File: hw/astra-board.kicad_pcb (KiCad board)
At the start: 2 copper layers, 60 x 40 mm, 53 parts, among them J1 USB-C, J2 QWIIC, J3 OLED, J4 EXPANSION, Q1 S8050, SW1 USER1, SW2 USER2, SW3 RESET, SW4 BOOT, U1 ESP32-C3-WROOM-02-N4, U2 AMS1117-3.3, U3 74AHCT1G125, U4 USBLC6-2SC6

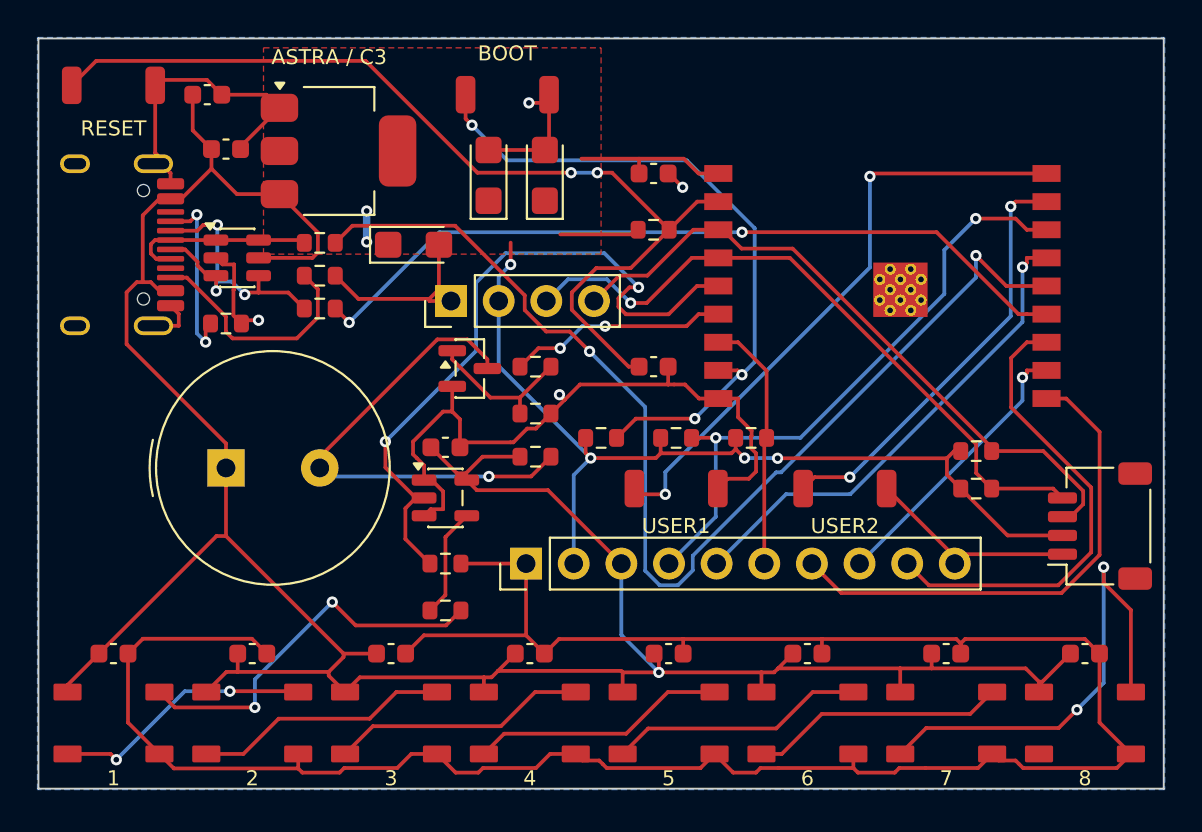
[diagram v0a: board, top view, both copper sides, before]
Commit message: Revise USB placement and power copper; regenerate verified fabrication package
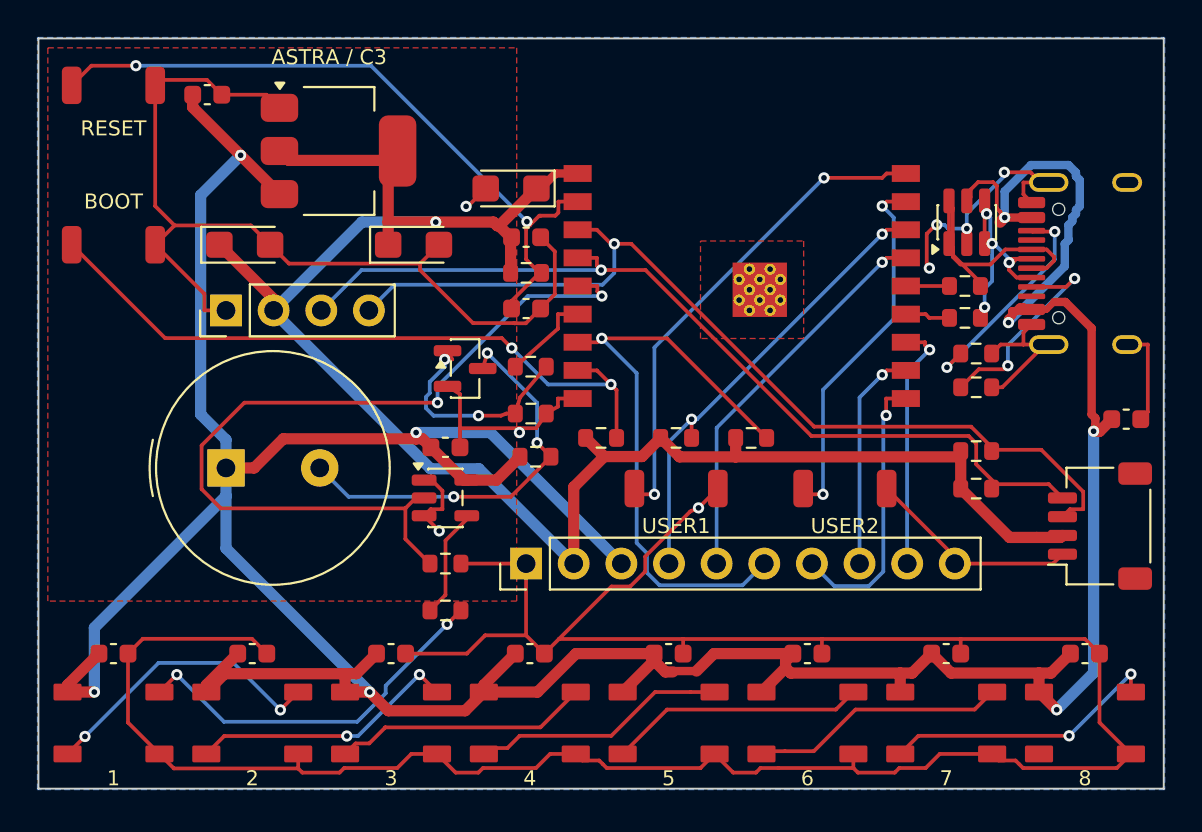
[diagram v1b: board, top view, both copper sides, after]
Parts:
- moved J1 54.0 mm to (157.0, 112.0), turned to 90 degrees
- moved C7 50.1 mm to (158.0, 120.3)
- moved R1 40.1 mm to (150.0, 118.6)
- moved U4 38.9 mm to (149.5, 109.8), turned to 90 degrees
- moved R2 35.2 mm to (150.0, 116.8)
- moved R14 34.5 mm to (149.4, 113.2), turned to 180 degrees
- moved R15 34.4 mm to (149.4, 114.9), turned to 180 degrees
- moved SW4 22.5 mm to (104.0, 111.0)
- moved C4 13.5 mm to (111.0, 111.0), turned to 0 degrees
- moved J3 12.0 mm to (110.0, 114.5)
- moved C1 7.60 mm to (126.0, 110.6)
- moved U1 7.50 mm to (137.5, 113.2)
- moved C2 7.47 mm to (126.0, 114.4)
- moved R3 7.18 mm to (126.0, 112.5)
- moved C5 1.93 mm to (125.2, 108.0), turned to 180 degrees
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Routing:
- net +5V: track 147.4 -> 208.0 mm, vias 1 -> 8
- net USB_P: track 60.9 -> 2.32 mm, vias 2 -> 0
- net USB_N: track 42.0 -> 2.41 mm, vias 2 -> 0
- net +3V3: track 65.4 -> 99.6 mm, vias 6 -> 1
- net GND: track 216.9 -> 244.4 mm, vias 4 -> 8
- net IO8: track 13.5 -> 32.9 mm, vias 0 -> 1
- net SDA: track 35.6 -> 50.5 mm, vias 0 -> 1
- net EN: track 51.7 -> 37.4 mm
- net SCL: track 35.7 -> 48.2 mm
- net IO10: track 27.0 -> 15.0 mm, vias 0 -> 1
- net TX: track 25.4 -> 13.4 mm, vias 0 -> 1
- net LED7: track 25.9 -> 15.0 mm
- net PIXEL: track 36.8 -> 45.2 mm
- net IO2: track 33.1 -> 24.8 mm
- net BUZZ: track 11.7 -> 4.87 mm, vias 2 -> 0
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- added copper zone on F.Cu, net GND
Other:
- board text added: "REV 1.1"
- board text removed: "REV 1.0"
